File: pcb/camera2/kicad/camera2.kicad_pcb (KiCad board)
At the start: 4 copper layers, 96.5 x 45.7 mm, 172 parts

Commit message: work
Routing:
- net out16P: vias 1 -> 0
- net out16N: vias 1 -> 0
- net out15P: vias 1 -> 0
- net out15N: vias 1 -> 0
- net out11P: vias 1 -> 0
- net out11N: vias 1 -> 0
- added copper zone on In1.Cu, net gnd
- added copper zone on In2.Cu, net vcc3_3in
- removed copper zone on In2.Cu, net gnd
- removed copper zone on In1.Cu, net vcc3_3in
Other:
- board text removed: "move CPLD down so that horizontal traces have to travel minimally"
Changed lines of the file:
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@@
     (area 101.524999 76.124999 198.195001 121.995001)
     (thickness 1.6)
-    (drawings 7)
-    (tracks 1040)
+    (drawings 6)
+    (tracks 1034)
     (zones 0)
     (modules 172)
@@
     (user_trace_width 1.524)
     (trace_clearance 0.127)
-    (zone_clearance 0.127)
+    (zone_clearance 0.254)
     (zone_45_only yes)
     (trace_min 0.127)
@@
     (effects (font (size 1.5 1.5) (thickness 0.3)))
   )
-  (gr_text "move CPLD down so that horizontal traces have to travel minimally" (at 202.81 59.54) (layer Dwgs.User)
-    (effects (font (size 1.5 1.5) (thickness 0.3)))
-  )
   (gr_text "connect shield on top too!" (at 152.67 74.52) (layer Dwgs.User)
     (effects (font (size 1.5 1.5) (thickness 0.3)))
@@
   (segment (start 190.207502 104.117502) (end 190.56 104.47) (width 0.1905) (layer F.Cu) (net 73))
   (segment (start 190.5587 104.4687) (end 190.56 104.47) (width 0.1905) (layer F.Cu) (net 73))
-  (via (at 190.56 104.47) (size 0.8636) (drill 0.508) (layers F.Cu B.Cu) (net 73))
   (segment (start 189.549864 104.4687) (end 190.5587 104.4687) (width 0.1905) (layer F.Cu) (net 73) (status 10))
   (segment (start 166.25 104.21) (end 184.51 104.21) (width 0.1905) (layer F.Cu) (net 74))
@@
   (segment (start 190.22 103.8) (end 190.57 103.45) (width 0.1905) (layer F.Cu) (net 74))
   (segment (start 190.5673 103.4527) (end 190.57 103.45) (width 0.1905) (layer F.Cu) (net 74))
-  (via (at 190.57 103.45) (size 0.8636) (drill 0.508) (layers F.Cu B.Cu) (net 74))
   (segment (start 189.481476 103.4527) (end 190.5673 103.4527) (width 0.1905) (layer F.Cu) (net 74) (status 10))
   (segment (start 158.388285 96.214732) (end 158.388285 96.348285) (width 0.1905) (layer F.Cu) (net 74) (status 30))
   (segment (start 158.388285 96.348285) (end 166.25 104.21) (width 0.1905) (layer F.Cu) (net 74) (status 10))
   (segment (start 166.83293 101.96293) (end 166.83293 101.819377) (width 0.1905) (layer F.Cu) (net 75) (status 30))
-  (via (at 190.56 101.42) (size 0.8636) (drill 0.508) (layers F.Cu B.Cu) (net 75))
   (segment (start 190.5593 101.4207) (end 190.56 101.42) (width 0.1905) (layer F.Cu) (net 75))
   (segment (start 190.21 101.77) (end 190.56 101.42) (width 0.1905) (layer F.Cu) (net 75))
@@
   (segment (start 190.5667 102.4367) (end 189.481476 102.4367) (width 0.1905) (layer F.Cu) (net 76) (status 20))
   (segment (start 166.593914 102.17293) (end 166.479377 102.17293) (width 0.1905) (layer F.Cu) (net 76) (status 30))
-  (via (at 190.57 102.44) (size 0.8636) (drill 0.508) (layers F.Cu B.Cu) (net 76))
   (segment (start 190.5667 102.4367) (end 190.57 102.44) (width 0.1905) (layer F.Cu) (net 76))
   (segment (start 190.217502 102.087502) (end 190.57 102.44) (width 0.1905) (layer F.Cu) (net 76))
@@
   (segment (start 190.217502 100.047502) (end 190.57 100.4) (width 0.1905) (layer F.Cu) (net 77))
   (segment (start 190.5653 100.4047) (end 190.57 100.4) (width 0.1905) (layer F.Cu) (net 77))
-  (via (at 190.57 100.4) (size 0.8636) (drill 0.508) (layers F.Cu B.Cu) (net 77))
   (segment (start 190.5653 100.4047) (end 189.481476 100.4047) (width 0.1905) (layer F.Cu) (net 77) (status 20))
   (segment (start 174.04 100.99) (end 175.3 99.73) (width 0.1905) (layer F.Cu) (net 78))
@@
   (segment (start 190.22 99.73) (end 190.56 99.39) (width 0.1905) (layer F.Cu) (net 78))
   (segment (start 190.5587 99.3887) (end 190.56 99.39) (width 0.1905) (layer F.Cu) (net 78))
-  (via (at 190.56 99.39) (size 0.8636) (drill 0.508) (layers F.Cu B.Cu) (net 78))
   (segment (start 190.5587 99.3887) (end 189.481476 99.3887) (width 0.1905) (layer F.Cu) (net 78) (status 20))
   (segment (start 162.90293 95.18293) (end 162.90293 95.049377) (width 0.1905) (layer F.Cu) (net 78) (status 30))
@@
   (via (at 178.16 91.17) (size 0.8636) (drill 0.508) (layers F.Cu B.Cu) (net 292))
   (segment (start 178.155164 91.174836) (end 178.16 91.17) (width 0.127) (layer F.Cu) (net 292))
-  (zone (net 1) (net_name gnd) (layer In2.Cu) (hatch edge 0.508)
+  (zone (net 92) (net_name vcc3_3in) (layer In2.Cu) (hatch edge 0.508)
     (connect_pads yes (clearance 0.254))
     (min_thickness 0.1524)
@@
     )
   )
-  (zone (net 92) (net_name vcc3_3in) (layer In1.Cu) (hatch edge 0.508)
+  (zone (net 1) (net_name gnd) (layer In1.Cu) (hatch edge 0.508)
     (connect_pads yes (clearance 0.127))
     (min_thickness 0.127)

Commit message: tmp
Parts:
- moved B20 13.0 mm to (168.4, 87.4)
- moved B1C 9.95 mm to (129.7, 90.4)
- moved B20C 9.21 mm to (171.6, 87.9), turned to 315 degrees
- moved B1 8.00 mm to (131.2, 87.5)
- moved B19C 2.33 mm to (165.1, 90.6)
- moved B18C 2.32 mm to (160.4, 88.6)
- moved B17C 2.29 mm to (164.0, 94.9)
- moved B11C 2.21 mm to (154.2, 93.8)
- moved B10C 2.09 mm to (144.6, 91.5)
- moved B6C 2.06 mm to (138.8, 94.4)
- moved B16C 2.04 mm to (158.8, 92.7)
- moved B2C 2.02 mm to (133.3, 88.9)
- moved B15C 1.99 mm to (162.7, 99.4)
- moved B5C 1.98 mm to (141.6, 88.3), turned to 90 degrees
- moved B4C 1.97 mm to (136.0, 91.7)
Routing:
- net pair14N: track 0.00 -> 22.8 mm, vias 0 -> 1
- net pair7N: track 0.00 -> 22.6 mm, vias 0 -> 1
- net pair13N: track 0.00 -> 21.7 mm, vias 0 -> 1
- net pair8N: track 0.00 -> 21.3 mm, vias 0 -> 1
- net pair12N: track 0.00 -> 20.4 mm, vias 0 -> 1
- net pair14P: track 0.00 -> 19.5 mm, vias 0 -> 1
- net pair7P: track 0.25 -> 19.6 mm, vias 0 -> 1
- net pair9N: track 0.00 -> 18.9 mm, vias 0 -> 1
- net pair8P: track 0.25 -> 18.3 mm, vias 0 -> 1
- net pair12P: track 0.25 -> 18.1 mm, vias 0 -> 1
- net pair13P: track 0.27 -> 17.6 mm, vias 0 -> 1
- net pair9P: track 0.00 -> 16.6 mm, vias 0 -> 1
- net vcc3_3in: track 16.0 -> 2.64 mm, vias 10 -> 1
- net pair20N: track 20.0 -> 6.73 mm
- net out20N: track 4.88 -> 17.7 mm
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
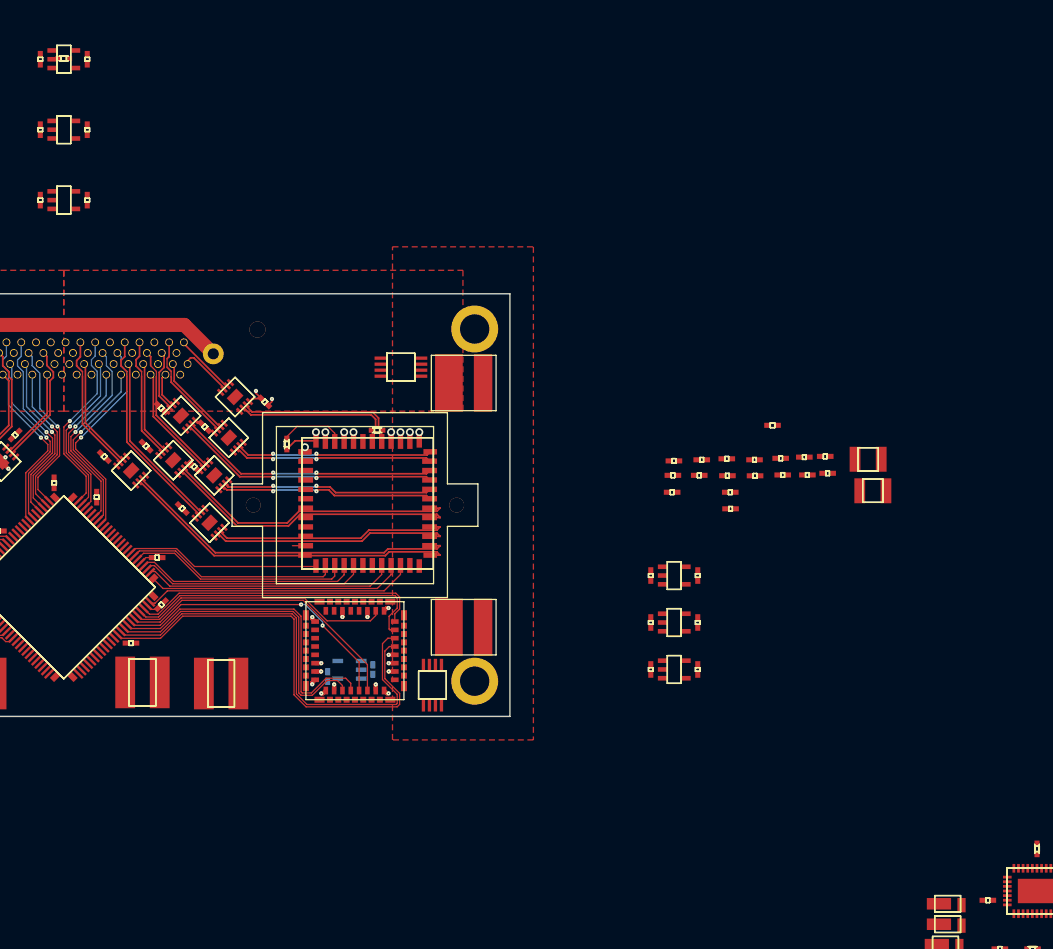
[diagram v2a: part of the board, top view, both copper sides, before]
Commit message: DRC passes. most everything routed except power and LEDs
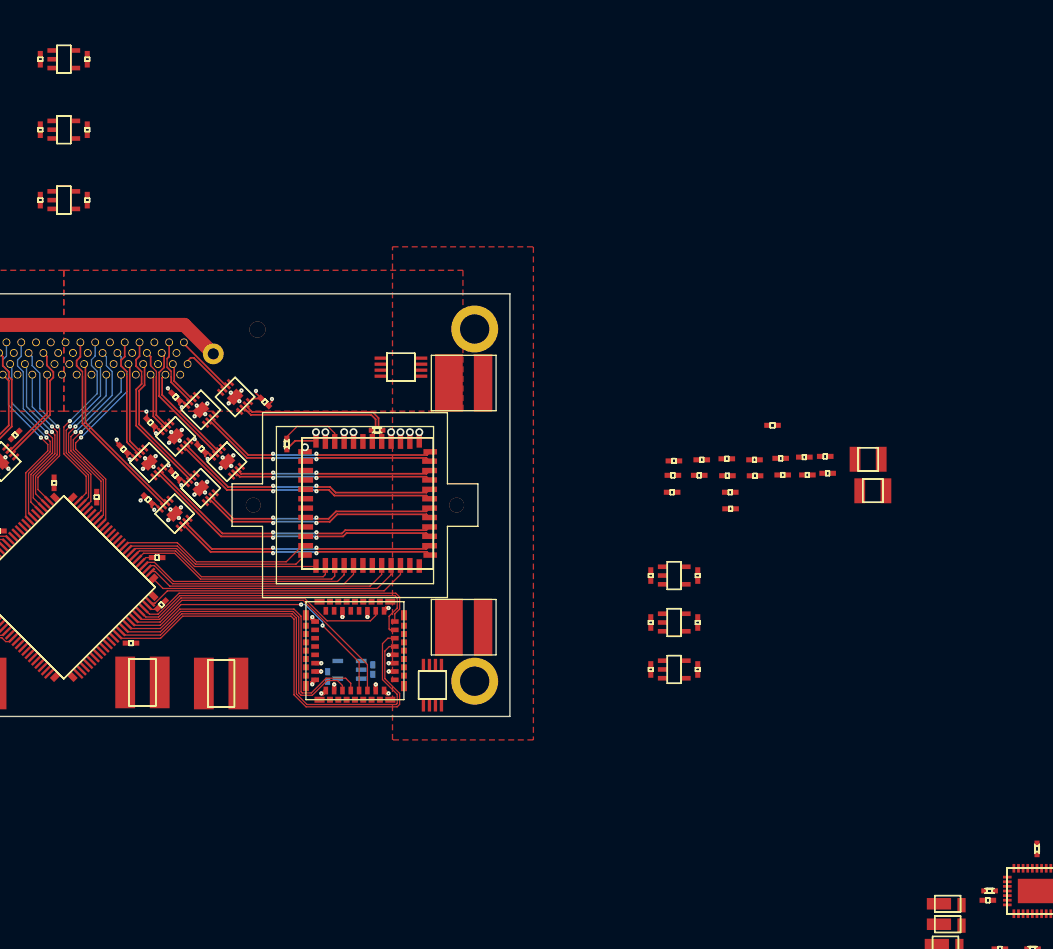
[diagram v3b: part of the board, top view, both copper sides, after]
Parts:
- moved IR3 134.7 mm to (250.0, 140.8), turned to 180 degrees
- moved B15 9.22 mm to (159.1, 94.5)
- moved B15C 9.02 mm to (156.3, 93.0)
- moved B18 7.03 mm to (167.5, 94.4)
- moved B17C 6.72 mm to (159.2, 90.1)
- moved B11C 6.63 mm to (159.0, 98.5)
- moved B11 6.62 mm to (161.8, 100.0)
- moved B18C 6.19 mm to (164.8, 93.0)
- moved B17 5.95 mm to (161.9, 91.6)
- moved B19C 4.51 mm to (162.0, 87.4)
- moved B16C 4.44 mm to (161.9, 95.8)
- moved B19 4.26 mm to (164.7, 88.8)
- moved B16 4.25 mm to (164.7, 97.2)
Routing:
- net gnd: track 62.1 -> 89.7 mm, vias 65 -> 99
- net C2trigger1: track 0.00 -> 20.6 mm
- net C2trigger0: track 1.38 -> 21.4 mm
- net vcc3_3in: track 2.64 -> 14.5 mm, vias 1 -> 7
- net pair15N: track 22.3 -> 13.1 mm
- net pair15P: track 19.3 -> 10.3 mm
- net out11P: track 37.0 -> 28.0 mm, vias 0 -> 2
- net out11N: track 37.1 -> 28.4 mm, vias 0 -> 2
- net pair18P: track 3.91 -> 11.0 mm
- net pair18N: track 6.71 -> 13.8 mm
- net out18N: track 28.6 -> 21.6 mm
- net out18P: track 28.3 -> 21.3 mm
- net out15N: track 26.0 -> 32.8 mm, vias 0 -> 2
- net out15P: track 25.7 -> 32.5 mm, vias 0 -> 2
- net pair11N: track 15.1 -> 21.8 mm
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
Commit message: CMOS decoupling figured out
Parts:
- removed the ID4D at (245.1, 149.3)
- removed the ID5D at (245.2, 146.6)
- removed the ID6D at (245.5, 144.4)
- removed the ID7D at (245.5, 142.2)
- removed the vcc1_2_1U at (117.8, 116.8)
- removed the vcc1_2_2U at (180.8, 116.9)
- removed the vcc1_8U at (149.9, 50.8)
- removed the vcc1_8_1U at (91.4, 94.0)
- removed the vcc1_8_2U at (215.9, 106.7)
- removed the vcc2_8U at (149.9, 58.5)
- removed the vcc3_0U at (149.9, 66.1)
- removed the vcc3_0_1aU at (91.4, 101.6)
- removed the vcc3_0_1bU at (91.4, 109.2)
- removed the vcc3_0_2aU at (215.9, 111.8)
- removed the vcc3_0_2bU at (215.9, 116.8)
- added ID4D: , gen:cbd95bc32455324305d8f308c2d74f4847a84f7577ba03a6430ffa7a2e3ad63b, F.Cu at (245.1, 149.3)
- added ID5D: , gen:cbd95bc32455324305d8f308c2d74f4847a84f7577ba03a6430ffa7a2e3ad63b, F.Cu at (245.2, 146.6)
- added ID6D: , gen:cbd95bc32455324305d8f308c2d74f4847a84f7577ba03a6430ffa7a2e3ad63b, F.Cu at (245.5, 144.4)
- added ID7D: , gen:cbd95bc32455324305d8f308c2d74f4847a84f7577ba03a6430ffa7a2e3ad63b, F.Cu at (245.5, 142.2)
- added P2: , gen:241492fd899311e7d9c7e61eadc180b241cdf3d88f3ef5a7a5d9a913c8bb5d54, F.Cu at (144.7, 97.0)
- added vcc1_2_1U: , gen:b59615b6c2f16aaf2cf9655964879d5a10751c3104015e0025f5e14f76c3b415, B.Cu at (117.8, 116.8)
- added vcc1_2_2U: , gen:b59615b6c2f16aaf2cf9655964879d5a10751c3104015e0025f5e14f76c3b415, B.Cu at (180.8, 116.9)
- added vcc1_8U: , gen:fc4e2d64400852a8763947ed47e4930b4253f45ce30e8508b335e36eb8ec984f, B.Cu at (144.7, 108.1)
- added vcc1_8_1U: , gen:fc4e2d64400852a8763947ed47e4930b4253f45ce30e8508b335e36eb8ec984f, F.Cu at (91.4, 94.0)
- added vcc1_8_2U: , gen:fc4e2d64400852a8763947ed47e4930b4253f45ce30e8508b335e36eb8ec984f, F.Cu at (215.9, 106.7)
- added vcc2_8U: , gen:d79d029443a7a676869eb4d5b0f7817e2790cd261f02f6e43eb3c9997e4695c5, F.Cu at (149.9, 58.5)
- added vcc3_0U: , gen:ffcbf41dc77fb2329a39ad51a1be56245199c75b7d3bee81ffc453dad97778b1, B.Cu at (153.7, 108.2)
- added vcc3_0_1aU: , gen:ffcbf41dc77fb2329a39ad51a1be56245199c75b7d3bee81ffc453dad97778b1, F.Cu at (91.4, 101.6)
- added vcc3_0_1bU: , gen:ffcbf41dc77fb2329a39ad51a1be56245199c75b7d3bee81ffc453dad97778b1, F.Cu at (91.4, 109.2)
- added vcc3_0_2aU: , gen:ffcbf41dc77fb2329a39ad51a1be56245199c75b7d3bee81ffc453dad97778b1, F.Cu at (215.9, 111.8)
- added vcc3_0_2bU: , gen:ffcbf41dc77fb2329a39ad51a1be56245199c75b7d3bee81ffc453dad97778b1, F.Cu at (215.9, 116.8)
- B1, B10, B11, B15, B16, B17, B18, B19, B2, B20, B3, B4, B5, B6: footprint gen:ec4c19d9976d47b7fe720a0af2fbe08b743ab89b55bf072d08ff9279dcf65392 -> gen:d5d747658d1f210c64ba5afe5344e053b8a2d55b6f3d730df7e8fcb94f698341
- C1C51, C1FB1, C2C51, C2FB1, vcc1_8C1, vcc1_8C2, vcc3_0C1, vcc3_0C2: moved to B.Cu
- C1C70, C1C71, C2C70, C2C71: footprint gen:3af735041c9a949bfeabfb85bc7bf975c38b0916fa7e7388b3919d993ce08374 -> gen:3908cb9356038a1f1fd88f53d6c520b8505039adcfdb7bb53781aaa6f96025d9; moved to B.Cu
- C1U1, C2U1: footprint gen:8f3aa85955296813636e406510ac2cb44b6b28d253d1e3863a516e66fbc77376 -> gen:2c43dbd9f6af1bb8faf0dc21f50b99c6562a4598033a204bce2cbb3aa0ac77e0
- IU3: footprint gen:10055cda59e5a70ce0bc86550a5f75ef499931ada32159cd6aabb90b37b327da -> gen:3cf7be2816aebb87938a72439acbc299fb39ba3576f28d4585b83a929bdf084e
- MU1: footprint gen:26b7ea9bab8162176cb957c507b2d408ca1ea6a8e21ee01cd2df422f221d0556 -> gen:090464809685175b38cabe7209672ac088d3c8d16318e2135ae4ec4fabcf0fdf
- P1: footprint gen:a1403a4ac11b1752655c81b77c786537d75d8acf64ea88171c3d4e9379b9cc3d -> gen:4d6fcb809a66ef36c471d0496d3ac88d05ca20df7fa16e20f1e1bc387cbd404d
- moved C1C12 89.6 mm to (124.8, 106.8), turned to 180 degrees
- moved C1C21 89.6 mm to (126.6, 106.2)
- moved C1C11 83.9 mm to (122.8, 91.0)
- moved C1C30 81.5 mm to (124.8, 91.0), turned to 180 degrees
- moved C1C31 81.1 mm to (119.7, 106.8), turned to 180 degrees
- moved C1C10 80.6 mm to (118.8, 91.0)
- moved C1C41 80.0 mm to (121.0, 106.9)
- moved C1C20 76.3 mm to (116.9, 91.0), turned to 180 degrees
- moved C1C51 75.9 mm to (124.8, 90.3), turned to 180 degrees
- moved C1FB1 74.5 mm to (118.4, 97.4), turned to 90 degrees
- moved C1C33 70.0 mm to (114.7, 91.0), turned to 180 degrees
- moved C1C32 69.5 mm to (111.8, 97.9), turned to 90 degrees
- moved C1C40 68.3 mm to (111.1, 97.9), turned to 90 degrees
- moved C1C60 66.1 mm to (111.8, 101.9), turned to 90 degrees
- moved C1C50 65.4 mm to (110.5, 97.9), turned to 90 degrees
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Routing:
- net gnd: track 89.7 -> 131.7 mm, vias 99 -> 121
- net C1MOSI: track 25.2 -> 4.56 mm
- net vcc3_0: track 4.42 -> 15.7 mm, vias 2 -> 7
- net cpld_TCK: track 0.00 -> 10.3 mm, vias 0 -> 1
- net vcc3_3in: track 14.5 -> 24.7 mm, vias 7 -> 10
- net vcc1_8: track 0.00 -> 9.81 mm, vias 0 -> 1
- net cpld_TDI: track 0.00 -> 7.76 mm, vias 0 -> 1
- net C1IBIAS: track 6.99 -> 0.00 mm
- net cpld_TMS: track 0.00 -> 6.77 mm, vias 0 -> 1
- net C2IBIAS: track 6.79 -> 7.59 mm
- net vcc3_0_2a: track 1.95 -> 1.22 mm, vias 2 -> 0
- net out4P: track 8.25 -> 8.90 mm
- net out5P: track 16.4 -> 17.1 mm
- net C2vdd_pix: track 0.49 -> 0.00 mm, vias 1 -> 0
- net vcc1_8_2: track 2.02 -> 2.51 mm, vias 2 -> 0
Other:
- board text added: "make sure shield decoupling is clear of connector"

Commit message: buffers finally finalized
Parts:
- vcc1_8_2C1, vcc1_8_2C2, vcc1_8_2U, vcc3_0_2aC1, vcc3_0_2aC2, vcc3_0_2aU, vcc3_0_2bC1, vcc3_0_2bC2, vcc3_0_2bU: moved to B.Cu
- moved vcc3_0_2bC2 44.3 mm to (180.8, 93.5), turned to 0 degrees
- moved vcc3_0_2bU 42.1 mm to (179.6, 95.5)
- moved vcc3_0_2aC2 40.0 mm to (183.1, 93.0)
- moved vcc3_0_2bC1 38.9 mm to (179.6, 97.5), turned to 0 degrees
- moved vcc3_0_2aU 35.6 mm to (185.7, 93.0), turned to 180 degrees
- moved vcc1_8_2C2 33.6 mm to (185.9, 98.0), turned to 180 degrees
- moved vcc3_0_2aC1 31.4 mm to (188.2, 93.0)
- moved vcc1_8_2U 30.6 mm to (185.9, 100.6), turned to 90 degrees
- moved vcc1_8_2C1 27.7 mm to (185.9, 103.1), turned to 180 degrees
- moved C2C70 4.02 mm to (178.8, 91.9), turned to 0 degrees
- moved C2FB1 3.71 mm to (178.6, 93.5), turned to 180 degrees
- moved B3 1.78 mm to (136.2, 90.1)
- moved B4C 1.69 mm to (134.8, 92.8)
- moved B4 1.58 mm to (133.4, 95.6)
- moved C2C71 1.57 mm to (178.6, 102.4), turned to 270 degrees
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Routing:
- net vcc3_3in: track 24.7 -> 34.3 mm, vias 10 -> 15
- net gnd: track 131.7 -> 124.3 mm, vias 121 -> 115
- net C1vdd_pix: track 4.38 -> 0.00 mm, vias 4 -> 0
- net vcc3_0_1a: track 3.67 -> 0.00 mm, vias 4 -> 0
- net vcc1_8_1: track 3.19 -> 0.00 mm, vias 3 -> 0
- net pair3N: track 6.82 -> 8.65 mm
- net pair3P: track 4.49 -> 6.33 mm
- net out3N: track 12.5 -> 10.8 mm
- net out3P: track 12.7 -> 11.0 mm
- net pair4N: track 14.5 -> 16.1 mm
- net pair4P: track 12.0 -> 13.7 mm
- net out4N: track 8.08 -> 6.49 mm
- net out4P: track 8.90 -> 7.32 mm
- net pair20P: track 5.88 -> 7.10 mm
- net out20N: track 17.7 -> 16.8 mm
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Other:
- board text removed: "connect shield on top too!"
- board text removed: "make sure shield decoupling is clear of connector"
- board text removed: "move clock in buffers to be with others"
